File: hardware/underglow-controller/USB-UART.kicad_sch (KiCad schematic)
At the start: 18 parts, among them J801 USB_C_Receptacle, Q801 BC817, Q802 BC817, U801 CP2102N-Axx-xQFN24

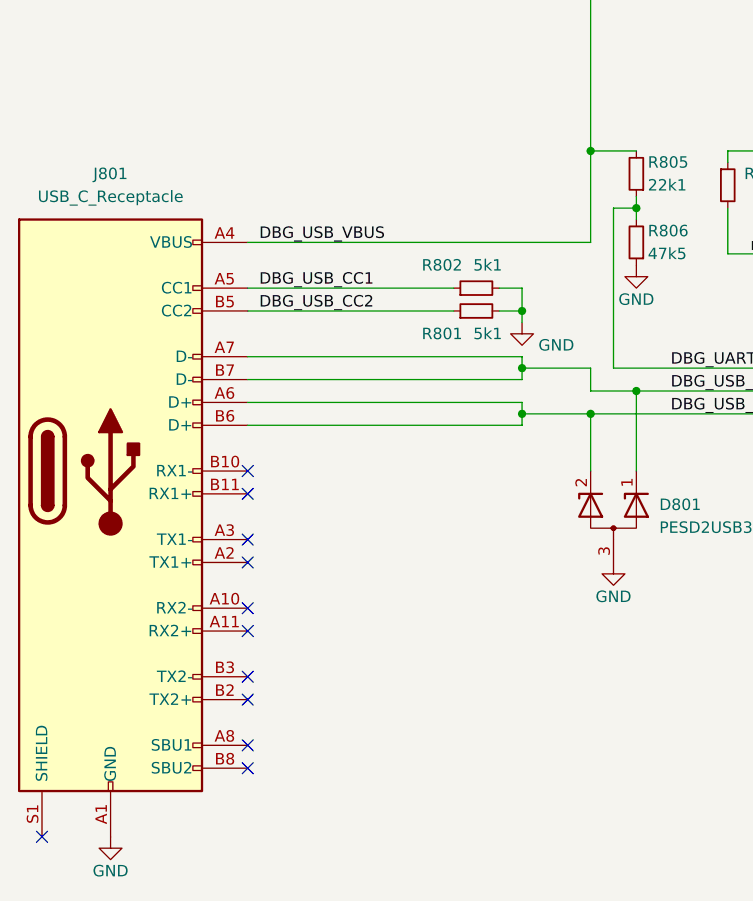
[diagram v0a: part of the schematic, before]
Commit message: more hardware updates. need to sort out the antenna for the radio  next
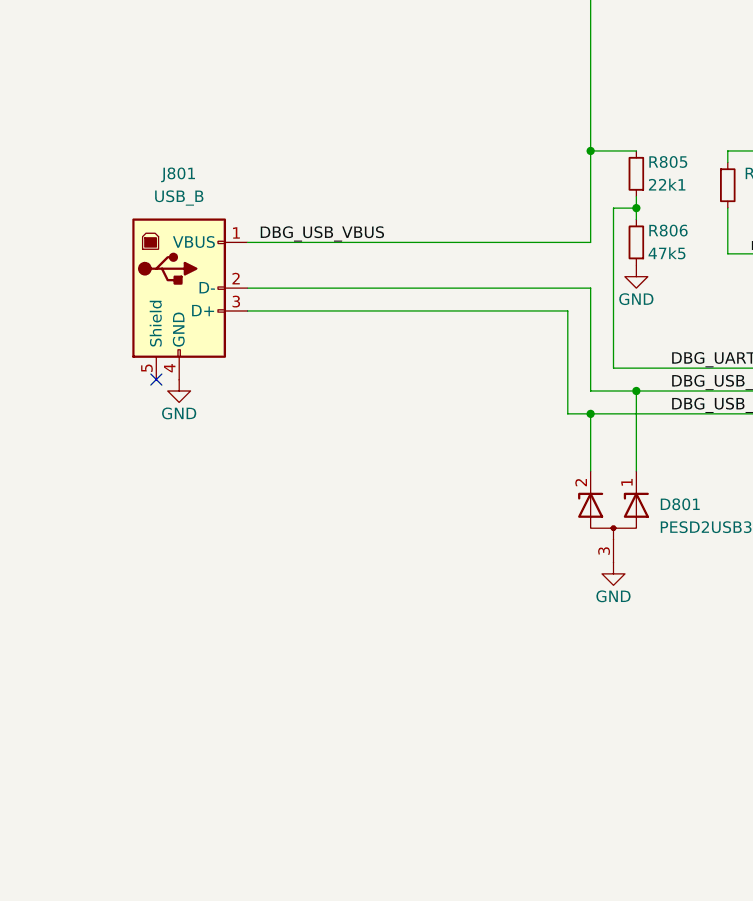
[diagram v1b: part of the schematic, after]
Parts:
- removed J801: USB_C_Receptacle, ConeCodes:CUI_UJ31-CH-3-MSMT-TR-67, symbol Connector:USB_C_Receptacle
- removed R801, R802: 5k1, Resistor_SMD:R_0402_1005Metric, symbol Device:R_Small
- added J801: USB_B, Connector_USB:USB_B_OST_USB-B1HSxx_Horizontal, symbol Connector:USB_B
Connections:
- net DBG_USB_D+: now also J801.3 (D+)
- net DBG_USB_D-: now also J801.2 (D-)
- net GND: now also J801.4 (GND)
- net VBUS: now also J801.1 (VBUS)
- no-connect marks 19 -> 9

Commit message: hardware: select some JLCPCB components
Signed-off-by: Connor Rigby <connorr@hey.com>
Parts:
- C802: Digikey (none) -> CGA2B1X7R1C104M050BC; MPN CGA2B1X7R1C104M050BC -> (none)
- D801: Digikey (none) -> PESD2USB3UV-T; MPN PESD2USB3UV-T -> (none)
- D802, D803: Digikey (none) -> QBLP601-2IR4; MPN QBLP601-2IR4 -> (none)
- R803, R804: Digikey (none) -> RMCF0402JT10K0; MPN RMCF0402JT10K0 -> (none)
- R807: Digikey (none) -> RMCF0402FT1K00; MPN RMCF0402FT1K00 -> (none)
- R808, R809: Digikey (none) -> RMCF0603JT240R; MPN RMCF0603JT240R -> (none)
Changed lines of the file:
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@@
       (effects (font (size 1.27 1.27)) hide)
     )
-    (property "MPN" "CGA2B1X7R1C104M050BC" (id 5) (at 179.07 44.45 0)
+    (property "Digikey" "CGA2B1X7R1C104M050BC" (id 5) (at 179.07 44.45 0)
       (effects (font (size 1.27 1.27)) hide)
     )
@@
       (effects (font (size 1.27 1.27)) hide)
     )
-    (property "MPN" "RMCF0402JT10K0" (id 5) (at 198.12 87.63 0)
+    (property "Digikey" "RMCF0402JT10K0" (id 5) (at 198.12 87.63 0)
       (effects (font (size 1.27 1.27)) hide)
     )
@@
       (effects (font (size 1.27 1.27)) hide)
     )
-    (property "MPN" "RMCF0402JT10K0" (id 5) (at 194.31 64.77 0)
+    (property "Digikey" "RMCF0402JT10K0" (id 5) (at 194.31 64.77 0)
       (effects (font (size 1.27 1.27)) hide)
     )
@@
       (effects (font (size 1.27 1.27)) hide)
     )
-    (property "MPN" "" (id 7) (at 173.99 44.45 0)
+    (property "Digikey" "" (id 7) (at 173.99 44.45 0)
       (effects (font (size 1.27 1.27)) hide)
     )
@@
       (effects (font (size 1.27 1.27)) hide)
     )
-    (property "MPN" "PESD2USB3UV-T" (id 4) (at 119.38 97.79 0)
+    (property "Digikey" "PESD2USB3UV-T" (id 4) (at 119.38 97.79 0)
       (effects (font (size 1.27 1.27)) hide)
     )
@@
       (effects (font (size 1.27 1.27)) hide)
     )
-    (property "MPN" "RMCF0402FT1K00" (id 5) (at 132.08 60.96 0)
+    (property "Digikey" "RMCF0402FT1K00" (id 5) (at 132.08 60.96 0)
       (effects (font (size 1.27 1.27)) hide)
     )
@@
       (effects (font (size 1.27 1.27)) hide)
     )
-    (property "MPN" "RMCF0603JT240R" (id 4) (at 182.88 101.6 0)
+    (property "Digikey" "RMCF0603JT240R" (id 4) (at 182.88 101.6 0)
       (effects (font (size 1.27 1.27)) hide)
     )
@@
       (effects (font (size 1.27 1.27)) hide)
     )
-    (property "MPN" "RMCF0603JT240R" (id 4) (at 182.88 99.06 0)
+    (property "Digikey" "RMCF0603JT240R" (id 4) (at 182.88 99.06 0)
       (effects (font (size 1.27 1.27)) hide)
     )
@@
       (effects (font (size 1.27 1.27)) hide)
     )
-    (property "MPN" "QBLP601-2IR4" (id 4) (at 203.2 102.87 0)
+    (property "Digikey" "QBLP601-2IR4" (id 4) (at 203.2 102.87 0)
       (effects (font (size 1.27 1.27)) hide)
     )
@@
       (effects (font (size 1.27 1.27)) hide)
     )
-    (property "MPN" "QBLP601-2IR4" (id 4) (at 203.2 97.79 0)
-      (effects (font (size 1.27 1.27)) hide)
-    )
+    (property "Digikey" "QBLP601-2IR4" (id 4) (at 203.2 97.79 0)
+      (effects (font (size 1.27 1.27)) hide)
+    )
